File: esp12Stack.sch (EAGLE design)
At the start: 23 parts, among them J02 470, J04 470, J05 470, J12 470, J13 470

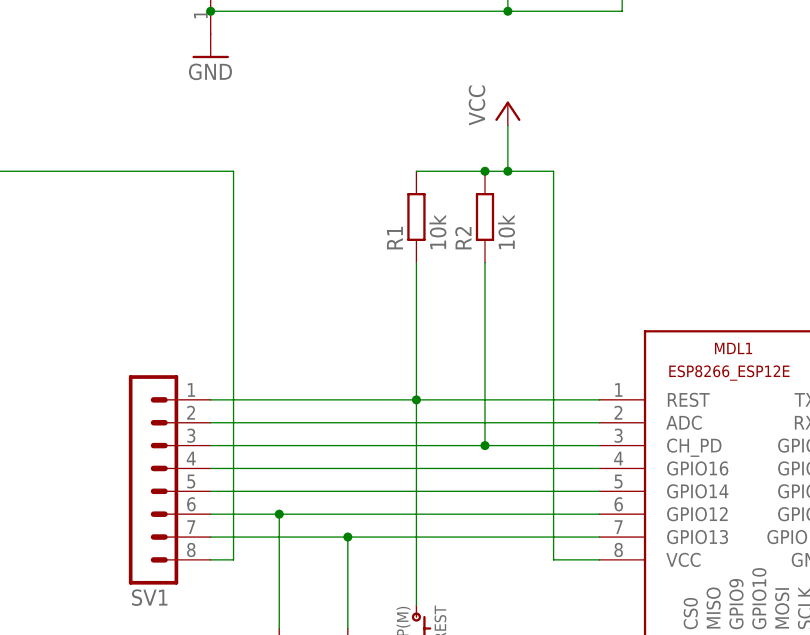
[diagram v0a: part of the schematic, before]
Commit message: Deep Sleep capability
added a jumper Position to connect GIPO16 and REST to enable wake up from deep sleep.
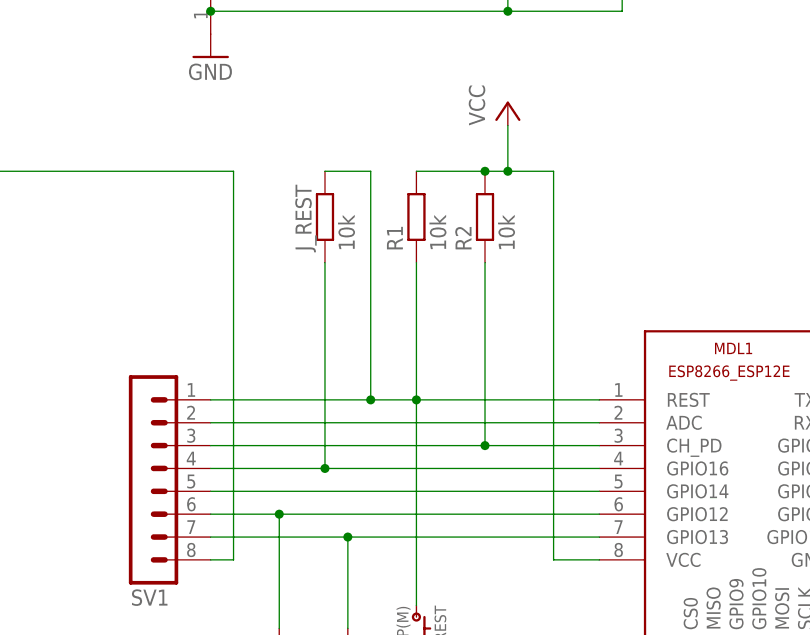
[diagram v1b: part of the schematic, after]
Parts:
- added J_REST: 10k, eagle-ltspice:R
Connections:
- net GPIO16: now also J_REST.1
- net REST: now also J_REST.2
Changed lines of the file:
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@@
 <part name="J13" library="eagle-ltspice" deviceset="R" device="" value="470"/>
 <part name="J12" library="eagle-ltspice" deviceset="R" device="" value="470"/>
+<part name="J_REST" library="eagle-ltspice" deviceset="R" device="" value="10k"/>
 </parts>
 <sheets>
@@
 <instance part="J13" gate="G$1" x="45.72" y="12.7" rot="R90"/>
 <instance part="J12" gate="G$1" x="38.1" y="12.7" rot="R90"/>
+<instance part="J_REST" gate="G$1" x="43.18" y="63.5" rot="R90"/>
 </instances>
 <busses>
@@
 <wire x1="73.66" y1="43.18" x2="53.34" y2="43.18" width="0.1524" layer="91"/>
 <pinref part="R1" gate="G$1" pin="1"/>
-<wire x1="53.34" y1="43.18" x2="30.48" y2="43.18" width="0.1524" layer="91"/>
+<wire x1="53.34" y1="43.18" x2="48.26" y2="43.18" width="0.1524" layer="91"/>
+<wire x1="48.26" y1="43.18" x2="30.48" y2="43.18" width="0.1524" layer="91"/>
 <wire x1="53.34" y1="58.42" x2="53.34" y2="43.18" width="0.1524" layer="91"/>
 <junction x="53.34" y="43.18"/>
 <wire x1="53.34" y1="43.18" x2="53.34" y2="20.32" width="0.1524" layer="91"/>
 <pinref part="REST" gate="G$1" pin="1"/>
+<pinref part="J_REST" gate="G$1" pin="2"/>
+<wire x1="43.18" y1="68.58" x2="48.26" y2="68.58" width="0.1524" layer="91"/>
+<wire x1="48.26" y1="68.58" x2="48.26" y2="43.18" width="0.1524" layer="91"/>
+<junction x="48.26" y="43.18"/>
 </segment>
 </net>
@@
 <pinref part="MDL1" gate="G$1" pin="GPIO16"/>
 <pinref part="SV1" gate="1" pin="4"/>
-<wire x1="73.66" y1="35.56" x2="30.48" y2="35.56" width="0.1524" layer="91"/>
+<wire x1="73.66" y1="35.56" x2="43.18" y2="35.56" width="0.1524" layer="91"/>
+<wire x1="43.18" y1="35.56" x2="30.48" y2="35.56" width="0.1524" layer="91"/>
+<wire x1="43.18" y1="35.56" x2="43.18" y2="58.42" width="0.1524" layer="91"/>
+<pinref part="J_REST" gate="G$1" pin="1"/>
+<junction x="43.18" y="35.56"/>
 </segment>
 </net>
